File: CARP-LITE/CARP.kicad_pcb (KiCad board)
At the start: 4 copper layers, 40 x 80 mm, 102 parts, among them J1 USB_C_Receptacle_USB2.0_14P, J10 PYRO_2, J2 SPI1+3V3, J3 I2C1+3V3, J4 2S XT30, J5 UART+5V+I2C1, J6 PYRO_1, J8 PWM1+6V, J9 PWM2+6V, Q5 SQ2318CES, Q6 SQ2318CES, Q7 SQ2318CES, SW1 SW_Push, SW2 SW_Push, U1 W25Q128JVSIMTR (16MB), U2 W25Q32RVXHJQ (2MB), U3 3V3 LDO, U4 RP2350_60QFN, U5 LSM6DSO, U6 BMP390, U7 5V LDO, U8 6V LDO, Y1 ABM8-272-T3

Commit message: radio idk
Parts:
- added C3: 100n, Capacitor_SMD:C_0603_1608Metric, F.Cu at (518.0, 236.6)
- added C36: 100n, Capacitor_SMD:C_0603_1608Metric, F.Cu at (518.0, 241.6)
- added C39: 470p, Capacitor_SMD:C_0402_1005Metric, F.Cu at (531.3, 236.3)
- added C4: 4.7u, Capacitor_SMD:C_0603_1608Metric, F.Cu at (518.0, 239.1)
- added C40: 6.8p, Capacitor_SMD:C_0402_1005Metric, F.Cu at (531.3, 238.3)
- added C41: 2.7p, Capacitor_SMD:C_0402_1005Metric, F.Cu at (531.3, 240.2)
- added C42: 1.1p, Capacitor_SMD:C_0402_1005Metric, F.Cu at (531.3, 242.2)
- added C43: 1.2p, Capacitor_SMD:C_0402_1005Metric, F.Cu at (531.3, 244.2)
- added C44: 2.0p, Capacitor_SMD:C_0402_1005Metric, F.Cu at (531.3, 246.1)
- added C45: 470p, Capacitor_SMD:C_0402_1005Metric, F.Cu at (534.1, 236.3)
- added C46: 11p, Capacitor_SMD:C_0402_1005Metric, F.Cu at (534.1, 238.3)
- added C47: 22p, Capacitor_SMD:C_0402_1005Metric, F.Cu at (534.1, 240.2)
- added C48: 5.6p, Capacitor_SMD:C_0402_1005Metric, F.Cu at (534.1, 242.2)
- added C49: 18p, Capacitor_SMD:C_0402_1005Metric, F.Cu at (534.1, 244.2)
- added C50: 10p, Capacitor_SMD:C_0402_1005Metric, F.Cu at (534.1, 246.1)
- added C51: 1.6p, Capacitor_SMD:C_0402_1005Metric, F.Cu at (537.0, 236.3)
- added C52: 47p, Capacitor_SMD:C_0402_1005Metric, F.Cu at (537.0, 238.3)
- added C53: 4.7u, Capacitor_SMD:C_0603_1608Metric, F.Cu at (518.0, 244.1)
- added C54: 4.7u, Capacitor_SMD:C_0603_1608Metric, F.Cu at (518.0, 246.6)
- added C55: 10p, Capacitor_SMD:C_0402_1005Metric, F.Cu at (537.0, 240.2)
- added C56: 4.7u, Capacitor_SMD:C_0603_1608Metric, F.Cu at (522.0, 236.6)
- added C57: 4.7u, Capacitor_SMD:C_0603_1608Metric, F.Cu at (522.0, 239.1)
- added FB1: 50@100M, Inductor_SMD:L_0603_1608Metric, F.Cu at (522.0, 241.6)
- added FB2: 50@100M, Inductor_SMD:L_0603_1608Metric, F.Cu at (522.0, 244.1)
- added FB3: 50@100M, Inductor_SMD:L_0603_1608Metric, F.Cu at (522.0, 246.6)
- added J11: RF_L, Connector_Coaxial:U.FL_Hirose_U.FL-R-SMT-1_Vertical, F.Cu at (532.5, 250.3)
- added J7: RF_H, Connector_Coaxial:U.FL_Hirose_U.FL-R-SMT-1_Vertical, F.Cu at (527.1, 250.3)
- added L10: 5.1n, Inductor_SMD:L_0402_1005Metric, F.Cu at (528.4, 238.3)
- added L11: 7.5n, Inductor_SMD:L_0402_1005Metric, F.Cu at (528.4, 240.3)
- added L12: 27n, Inductor_SMD:L_0402_1005Metric, F.Cu at (528.4, 242.3)
- added L13: 75n, Inductor_SMD:L_0402_1005Metric, F.Cu at (528.4, 244.3)
- added L2: 4.7u, Inductor_SMD:L_0805_2012Metric, F.Cu at (526.3, 254.7)
- added L3: 2.4n, Inductor_SMD:L_0402_1005Metric, F.Cu at (525.5, 236.3)
- added L4: 18n, Inductor_SMD:L_0402_1005Metric, F.Cu at (525.5, 238.3)
- added L5: 1.5n, Inductor_SMD:L_0402_1005Metric, F.Cu at (525.5, 240.3)
- added L6: 1.9n, Inductor_SMD:L_0402_1005Metric, F.Cu at (525.5, 242.3)
- added L7: 1.1n, Inductor_SMD:L_0402_1005Metric, F.Cu at (525.5, 244.3)
- added L8: 22n, Inductor_SMD:L_0402_1005Metric, F.Cu at (525.5, 246.2)
- added L9: 10n, Inductor_SMD:L_0402_1005Metric, F.Cu at (528.4, 236.3)
- added U9: LR2021IMLTRT, Package_DFN_QFN:QFN-32-1EP_5x5mm_P0.5mm_EP3.7x3.7mm_ThermalVias, F.Cu at (520.0, 251.5)
- added Y2: TG2520SMN-32.0000M-MCGNNM0, Oscillator:Oscillator_SMD_ECS_2520MV-xxx-xx-4Pin_2.5x2.0mm, F.Cu at (530.5, 255.4)
- J1: value USB_C_Receptacle_USB2.0_14P -> USB-C
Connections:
- J1 pad A8: (no net) -> unconnected-(J1-SBU1-PadA8)
- J1 pad B8: (no net) -> unconnected-(J1-SBU2-PadB8)
- J1 pad SH: (no net) -> GND

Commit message: Update button footprint to proper one
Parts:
- added FB1: 60@100M, Inductor_SMD:L_0603_1608Metric, F.Cu at (554.0, 236.0)
- FB2: value 50@100M -> 60@100M
- SW1, SW2: footprint Button_Switch_SMD:SW_Push_1P1T_NO_Vertical_Wuerth_434133025816 -> Button_Switch_SMD:SW_Push_1P1T_XKB_TS-1187A
- moved L2 17.8 mm to (543.0, 248.4)
- moved C3 17.8 mm to (534.7, 230.3)
- moved C53 17.8 mm to (534.7, 237.8)
- moved C56 17.8 mm to (538.7, 230.3)
- moved FB2 17.8 mm to (538.7, 237.8)
- moved L11 17.8 mm to (545.1, 234.0)
- moved L5 17.8 mm to (542.2, 234.0)
- moved L8 17.8 mm to (542.2, 240.0)
- moved C36 17.8 mm to (534.7, 235.3)
- moved C39 17.8 mm to (548.0, 230.1)
- moved C4 17.8 mm to (534.7, 232.8)
- moved C40 17.8 mm to (548.0, 232.0)
- moved C41 17.8 mm to (548.0, 234.0)
- moved C42 17.8 mm to (548.0, 236.0)
- moved C43 17.8 mm to (548.0, 237.9)
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
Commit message: do pyro shebang and pcb work
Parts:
- removed the FB1 at (538.7, 235.3)
- removed J2: SPI1+3V3, Connector_Molex:Molex_PicoBlade_53047-0610_1x06_P1.25mm_Vertical
- removed JP1: SolderJumper_3_Bridged12, Jumper:SolderJumper-3_P1.3mm_Bridged12_RoundedPad1.0x1.5mm_NumberLabels
- R24, R25, R26, R31, R32, R33, R34, R35: footprint Resistor_SMD:R_0603_1608Metric -> Resistor_SMD:R_0402_1005Metric
- R27, R28, R29, R30: footprint Resistor_SMD:R_0402_1005Metric_Pad0.72x0.64mm_HandSolder -> Jumper:SolderJumper-2_P1.3mm_Bridged_RoundedPad1.0x1.5mm
- moved TP1 168.0 mm to (366.2, 265.0)
- moved TP2 168.0 mm to (366.2, 268.6)
- moved TP3 168.0 mm to (366.2, 272.1)
- moved L2 160.1 mm to (430.9, 362.7)
- moved C3 160.1 mm to (422.6, 344.6)
- moved C36 160.1 mm to (422.6, 349.6)
- moved C4 160.1 mm to (422.6, 347.1)
- moved C43 160.1 mm to (435.9, 352.2)
- moved C49 160.1 mm to (438.7, 352.2)
- moved C53 160.1 mm to (422.6, 352.1)
- moved C56 160.1 mm to (426.6, 344.6)
- moved FB1 160.1 mm to (441.8, 350.3)
- moved J11 160.1 mm to (437.1, 358.3)
- moved J7 160.1 mm to (431.7, 358.3)
- moved L3 160.1 mm to (430.1, 344.4)
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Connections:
- U6 pad 5: Net-(JP1-C) -> GND
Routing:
- net +2S: track 0.00 -> 24.1 mm
- net +6V: track 15.0 -> 0.00 mm
- net /GPIO28: track 0.00 -> 6.97 mm
- net /GPIO29: track 0.00 -> 6.83 mm
- net Net-(J6-Pin_2): track 0.00 -> 6.17 mm
- net Net-(J10-Pin_2): track 0.00 -> 6.12 mm
- net /GPIO21: track 0.00 -> 4.79 mm
- net /GPIO22: track 0.00 -> 4.41 mm
- net Net-(Q5-G): track 0.00 -> 4.38 mm
- net Net-(Q6-G): track 0.00 -> 4.32 mm
- net GND: track 0.00 -> 2.23 mm, vias 4 -> 24
- removed copper zone on In2.Cu, net +3V3
- removed copper zone on B.Cu, net GND
- removed copper zone on In1.Cu, net GND
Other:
- board size 40 x 80 mm -> 77.1 x 100.6 mm
- board text added: "GNSS"
- board text added: "I2C1"
- board text added: "PWM1"
- board text added: "PWM2"

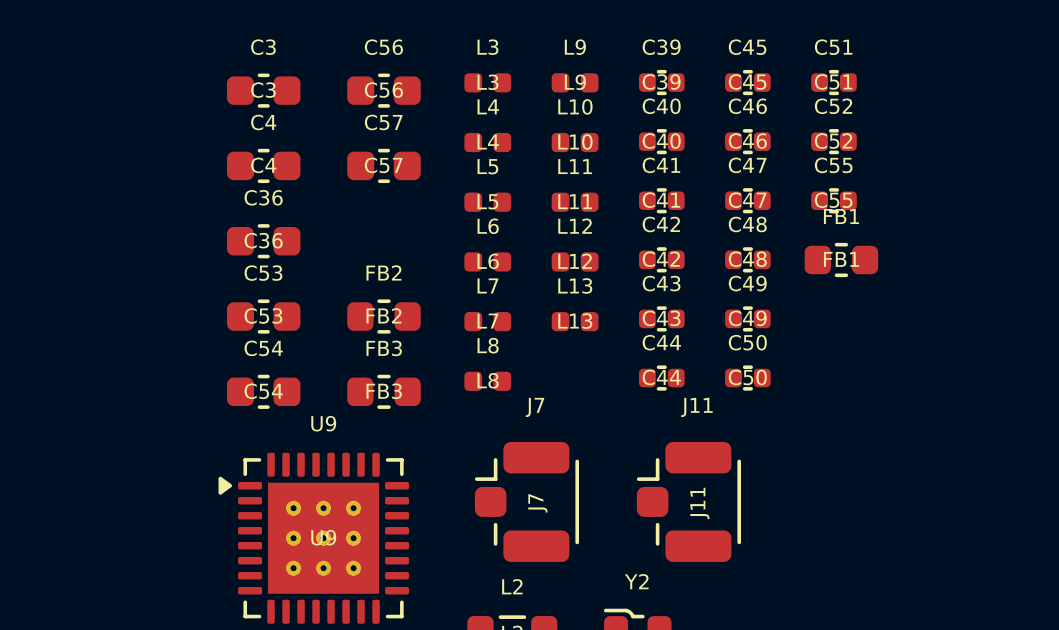
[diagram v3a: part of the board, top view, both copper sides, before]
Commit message: move stuff around
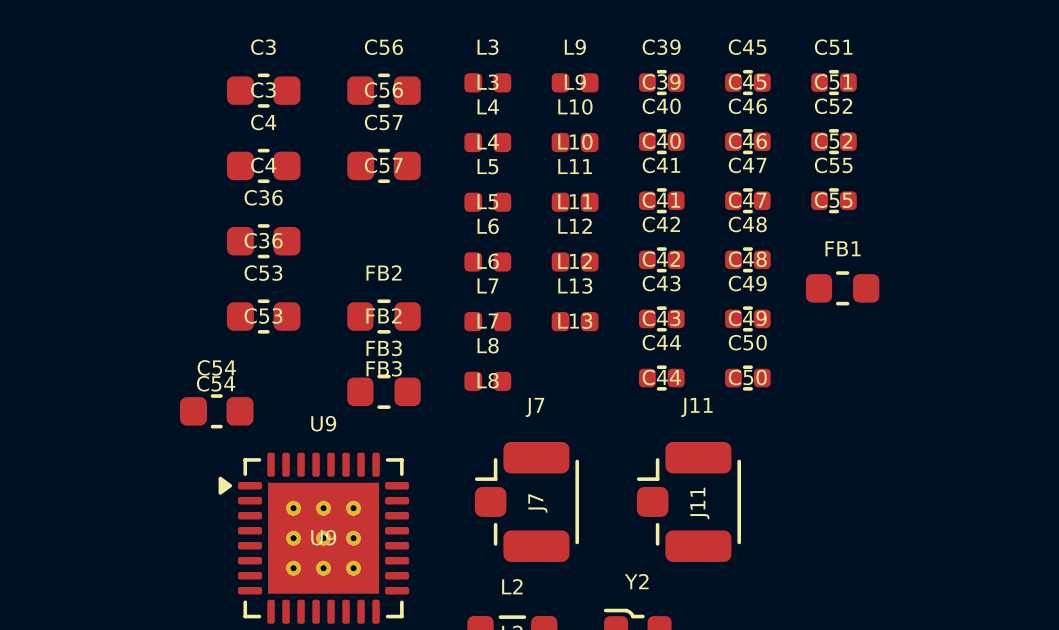
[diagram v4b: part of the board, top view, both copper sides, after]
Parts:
- moved C54 1.69 mm to (421.0, 355.3)
- moved FB1 0.95 mm to (441.9, 351.2)
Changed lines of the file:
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@@
 		)
 		(fp_text user "${REFERENCE}"
-			(at 0 0 0)
+			(at 0 -0.75 0)
 			(layer "F.SilkS")
 			(effects
@@
 	(footprint "Inductor_SMD:L_0603_1608Metric"
 		(layer "F.Cu")
-		(at 441.8475 350.255)
+		(at 441.8875 351.2)
 		(descr "Inductor SMD 0603 (1608 Metric), square (rectangular) end terminal, IPC-7351 nominal, (Body size source: http://www.tortai-tech.com/upload/download/2011102023233369053.pdf)")
 		(tags "inductor")
 		(property "Reference" "FB1"
-			(at 0 -1.43 0)
+			(at 0.0125 -1.3 0)
 			(layer "F.SilkS")
 			(effects
@@
 			(layer "F.Fab")
 		)
-		(fp_text user "${REFERENCE}"
-			(at 0 0 0)
-			(layer "F.SilkS")
-			(effects
-				(font
-					(size 0.5 0.5)
-				)
-			)
-		)
 		(pad "1" smd roundrect
 			(at -0.7875 0)
@@
 	(footprint "Capacitor_SMD:C_0603_1608Metric"
 		(layer "F.Cu")
-		(at 422.59 354.65)
+		(at 421.025 355.3)
 		(descr "Capacitor SMD 0603 (1608 Metric), square (rectangular) end terminal, IPC-7351 nominal, (Body size source: IPC-SM-782 page 76, https://www.pcb-3d.com/wordpress/wp-content/uploads/ipc-sm-782a_amendment_1_and_2.pdf)")
 		(tags "capacitor")
@@
 		)
 		(fp_text user "${REFERENCE}"
-			(at 0 0 0)
+			(at -0.025 -0.9 0)
 			(layer "F.SilkS")
 			(effects

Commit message: power delivery revamp
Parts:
- added C58: 22u, Capacitor_SMD:C_0805_2012Metric, F.Cu at (441.2, 247.0)
- added C59: 620p, Capacitor_SMD:C_0402_1005Metric, F.Cu at (440.4, 256.1)
- added C60: 10u, Capacitor_SMD:C_0805_2012Metric, F.Cu at (441.2, 250.0)
- added L14: 2.2u, Inductor_SMD:L_Coilcraft_XxL4020, F.Cu at (446.2, 253.6)
- added TP1: TestPoint, TestPoint:TestPoint_Pad_D1.5mm, F.Cu at (440.8, 253.3)
- added U10: TPS62130A, Package_DFN_QFN:VQFN-16-1EP_3x3mm_P0.5mm_EP1.68x1.68mm_ThermalVias, F.Cu at (446.5, 248.2)
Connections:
- R16 pad 1: /VBUS -> +5V

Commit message: nothing specific
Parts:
- removed C30: 1000u, Capacitor_SMD:CP_Elec_10x10
- removed C34: 10u, Capacitor_SMD:C_0603_1608Metric
- removed the TP1 at (366.2, 265.0)
- removed U7: 5V LDO, Package_TO_SOT_SMD:SOT-223-3_TabPin2
- removed U8: 6V LDO, Package_TO_SOT_SMD:SOT-223-3_TabPin2
- added C37: 100n, Capacitor_SMD:C_0603_1608Metric, F.Cu at (395.9, 239.1)
- added C38: 18p, Capacitor_SMD:C_0402_1005Metric, F.Cu at (395.4, 241.3)
- added C61: 22u, Capacitor_SMD:C_0805_2012Metric, F.Cu at (304.8, 188.5)
- added C62: 22u, Capacitor_SMD:C_0805_2012Metric, F.Cu at (304.8, 191.5)
- added C63: 220u, Capacitor_Tantalum_SMD:CP_EIA-7343-31_Kemet-D, F.Cu at (378.5, 252.4)
- added C64: 68u, Capacitor_Tantalum_SMD:CP_EIA-3528-21_Kemet-B, F.Cu at (386.5, 252.1)
- added D3: V2FL45, Diode_SMD:D_SMF, F.Cu at (284.5, 233.9)
- added D4: VSSAF5L45, Diode_SMD:D_SMA, F.Cu at (310.4, 219.7)
- added D5: BAS40LTH, Diode_SMD:D_SOD-882, F.Cu at (390.6, 255.4)
- added R23: 100k, Resistor_SMD:R_0603_1608Metric, F.Cu at (300.6, 188.2)
- added R36: 976k, Resistor_SMD:R_0603_1608Metric, F.Cu at (300.6, 190.8)
- added R37: 180k, Resistor_SMD:R_0603_1608Metric, F.Cu at (300.6, 193.3)
- C26: value 100u -> 22u; footprint Capacitor_SMD:C_0603_1608Metric -> Capacitor_SMD:C_0805_2012Metric
- C28, C35: value 10u -> 220u; footprint Capacitor_SMD:C_0603_1608Metric -> Capacitor_Tantalum_SMD:CP_EIA-7343-31_Kemet-D
- C59: footprint Capacitor_SMD:C_0402_1005Metric -> Capacitor_SMD:C_0603_1608Metric
- C60: value 10u -> 22u
- C7: value 10u -> 22u; footprint Capacitor_SMD:C_0603_1608Metric -> Capacitor_SMD:C_0805_2012Metric
- J8: value PWM1+6V -> PWM1+5V1
- J9: value PWM2+6V -> PWM2+5V1
- R16: value 5.1k -> 1k
- R19, R20, R21, R22, R24, R25, R26, R31, R32, R33, R34, R35, R4, R5, R8: footprint Resistor_SMD:R_0402_1005Metric -> Resistor_SMD:R_0603_1608Metric
- U6: footprint footprints:10LGA_2X2X0p75_BOS -> bmp_fps:10LGA_2X2X0p75_BOS
- moved U10 143.4 mm to (315.5, 189.9)
- moved J4 143.3 mm to (314.6, 182.8)
- moved C58 137.2 mm to (313.8, 196.1)
- moved C59 137.2 mm to (313.0, 205.1)
- moved C60 137.2 mm to (313.8, 199.1)
- moved L14 137.2 mm to (318.8, 202.7)
- moved TP1 137.2 mm to (313.4, 202.3)
- moved U3 124.0 mm to (303.1, 201.3)
- moved C35 87.2 mm to (378.5, 246.6)
- moved C28 29.5 mm to (378.5, 240.7)
- moved C27 25.0 mm to (467.9, 285.6)
- moved C31 25.0 mm to (467.2, 279.7)
- moved C33 25.0 mm to (467.9, 277.8)
- moved J10 25.0 mm to (472.4, 275.9)
- moved J6 25.0 mm to (472.3, 283.9)
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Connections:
- C28 pad 1: +2S -> +5V
- C35 pad 1: Net-(D4-A) -> Net-(J8-Pin_3)
- J8 pad 3: +6V -> Net-(J8-Pin_3)
- J9 pad 3: +6V -> +5V1

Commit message: pcb work
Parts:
- R17, R18, R19, R20, R21, R22, R24, R25, R26, R31, R33, R34, R35, R4, R5, R8: footprint Resistor_SMD:R_0603_1608Metric -> Resistor_SMD:R_0402_1005Metric
- R29, R30: moved to B.Cu
- moved D3 167.2 mm to (443.3, 286.2), turned to -90 degrees
- moved J4 143.0 mm to (429.4, 268.0)
- moved C37 135.7 mm to (443.0, 366.4)
- moved C60 125.3 mm to (420.3, 265.0), turned to -90 degrees
- moved C38 120.6 mm to (441.7, 352.7)
- moved R15 100.6 mm to (375.9, 298.8), turned to 90 degrees
- moved Q7 91.2 mm to (376.9, 295.2), turned to 90 degrees
- moved R14 89.8 mm to (377.9, 298.8), turned to -90 degrees
- moved BZ1 87.6 mm to (388.8, 296.8), turned to 180 degrees
- moved R27 87.3 mm to (463.9, 269.1), turned to 180 degrees
- moved R28 84.2 mm to (459.9, 283.0), turned to 180 degrees
- moved R30 64.0 mm to (439.8, 266.9)
- moved R29 63.0 mm to (439.6, 274.5)
- moved C29 59.4 mm to (464.6, 265.5), turned to -90 degrees
- moved D2 52.9 mm to (439.7, 282.5)
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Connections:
- C31 pad 2: /GPIO28 -> /GPIO28_ADC2
- C32 pad 2: /GPIO29 -> /GPIO29_ADC3
- R24 pad 1: /GPIO28 -> /GPIO28_ADC2
- R26 pad 2: /GPIO28 -> /GPIO28_ADC2
- R32 pad 1: /GPIO29 -> /GPIO29_ADC3
- R34 pad 2: /GPIO29 -> /GPIO29_ADC3
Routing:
- net Net-(U4-GPIO29_ADC3): track 0.00 -> 33.7 mm, vias 0 -> 1
- net /QSPI_SD3: track 0.00 -> 31.2 mm
- net /GPIO2: track 0.00 -> 27.2 mm
- net /GPIO3: track 0.00 -> 27.1 mm
- net Net-(U4-GPIO28_ADC2): track 0.00 -> 26.1 mm, vias 0 -> 1
- net /QSPI_SD0: track 0.00 -> 24.0 mm, vias 0 -> 2
- net /RUN: track 0.00 -> 23.3 mm
- net +3V3: track 0.00 -> 21.0 mm, vias 0 -> 18
- net /GPIO21: track 4.79 -> 25.8 mm, vias 0 -> 2
- net /QSPI_SD2: track 0.00 -> 21.0 mm
- net /QSPI_SCLK: track 0.00 -> 18.9 mm
- net /USB_D-: track 0.00 -> 15.2 mm
- net /USB_D+: track 0.00 -> 15.2 mm
- net /QSPI_SD1: track 0.00 -> 13.4 mm
- net Net-(J1-CC1): track 0.00 -> 11.4 mm
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- added copper zone on In2.Cu, net +3V3
- added copper zone on B.Cu, net GND
- added copper zone on In1.Cu, net GND

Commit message: buck
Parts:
- moved TP1 115.3 mm to (418.8, 281.4)
- moved C58 112.4 mm to (414.9, 277.6), turned to 180 degrees
- moved C59 112.0 mm to (423.1, 275.7), turned to 0 degrees
- moved U10 111.8 mm to (420.6, 272.4)
- moved L14 110.4 mm to (415.7, 270.4), turned to 180 degrees
- moved R37 107.6 mm to (420.0, 275.7)
- moved R23 106.8 mm to (416.7, 273.6)
- moved R36 106.6 mm to (416.7, 275.7)
- moved D4 105.9 mm to (420.4, 278.2)
- moved C61 102.2 mm to (414.2, 274.6), turned to -90 degrees
- moved C62 96.4 mm to (415.5, 266.9)
- moved C63 36.5 mm to (399.4, 282.4), turned to 90 degrees
- moved C35 28.0 mm to (404.8, 291.2), turned to 90 degrees
- moved C60 2.86 mm to (420.1, 267.9)
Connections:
- C35 pad 1: Net-(J8-Pin_3) -> +5V1
- J8 pad 3: Net-(J8-Pin_3) -> +5V1
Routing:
- net +5V1: track 0.01 -> 11.7 mm
- net GND: track 9.59 -> 4.59 mm, vias 63 -> 62
- net +2S: track 14.2 -> 9.26 mm
- net Net-(U10-FB): track 0.00 -> 3.96 mm
- net Net-(U10-PG): track 0.00 -> 1.82 mm
- net Net-(U10-SS/TR): track 1.69 -> 3.28 mm
- added copper zone on F.Cu, net +2S
- added copper zone on F.Cu, net +5V1
- added copper zone on F.Cu, net Net-(L14-Pad1)
